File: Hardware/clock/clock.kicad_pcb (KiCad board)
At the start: 2 copper layers, 127.5 x 48 mm, 19 parts, among them J1 Barrel_Jack_Switch, U1 WEMOS_C3_mini, U2 MAX7221xNG, U3 SBC18-11EGWA, U4 LM2596S-5, U5 SBC18-11EGWA, U6 SBC18-11EGWA, U7 SBC18-11EGWA

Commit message: Refactor code structure for improved readability and maintainability
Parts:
- added C10: 100nF, SparkFun-Capacitor:C_0805_2012Metric, B.Cu at (85.8, 122.1)
- added C11: 100nF, SparkFun-Capacitor:C_0805_2012Metric, B.Cu at (164.4, 138.2)
- added C12: 100nF, SparkFun-Capacitor:C_0805_2012Metric, B.Cu at (125.6, 125.6)
- added C6: 100nF, SparkFun-Capacitor:C_0805_2012Metric, B.Cu at (99.5, 110.2)
- added C7: 22uF, Capacitor_SMD:C_0805_2012Metric_Pad1.18x1.45mm_HandSolder, B.Cu at (168.0, 130.8)
- added C8: 100nF, SparkFun-Capacitor:C_0805_2012Metric, B.Cu at (169.0, 128.2)
- added C9: 220uF, Capacitor_THT:C_Radial_D6.3mm_H5.0mm_P2.50mm, B.Cu at (87.1, 126.7)
- added J2: Conn_02x03_Top_Bottom, Connector_IDC:IDC-Header_2x03_P2.54mm_Horizontal, B.Cu at (157.3, 141.3)
- added Q1: BC817, Package_TO_SOT_SMD:SOT-23, B.Cu at (163.4, 130.6)
- added Q2: BC817, Package_TO_SOT_SMD:SOT-23, B.Cu at (154.6, 130.6)
- added R2: 10kΩ, PCM_JLCPCB:R_0805, B.Cu at (158.8, 129.4)
- added R3: 10kΩ, PCM_JLCPCB:R_0805, B.Cu at (158.9, 131.8)
- added R4: 10kΩ, PCM_JLCPCB:R_0805, B.Cu at (164.3, 135.4)
- added REF**: MountingHole_2.2mm_M2_Pad_Via, MountingHole:MountingHole_2.2mm_M2_Pad_Via, F.Cu at (171.2, 144.0)
- added REF**: MountingHole_2.2mm_M2_Pad_Via, MountingHole:MountingHole_2.2mm_M2_Pad_Via, F.Cu at (45.1, 95.7)
- added REF**: MountingHole_2.2mm_M2_Pad_Via, MountingHole:MountingHole_2.2mm_M2_Pad_Via, F.Cu at (171.3, 95.9)
- added REF**: MountingHole_2.2mm_M2_Pad_Via, MountingHole:MountingHole_2.2mm_M2_Pad_Via, F.Cu at (45.5, 143.7)
- added SW1: PTH_RA_h7.5mm, SparkFun-Switch:Push_PTH_RA_8-020_h7.5mm, B.Cu at (171.4, 136.9)
- added U8: LM2596S-5, Package_TO_SOT_SMD:TO-263-5_TabPin3, B.Cu at (52.8, 121.8)
- C1: value 680uF -> 10uF; footprint Capacitor_THT:C_Radial_D8.0mm_H11.5mm_P3.50mm -> Capacitor_SMD:CP_Elec_4x5.4
- C2: value 220uF -> 100nF; footprint Capacitor_THT:C_Radial_D6.3mm_H5.0mm_P2.50mm -> SparkFun-Capacitor:C_0805_2012Metric
- C3: value 104 -> 680uF; footprint Capacitor_THT:C_Disc_D3.0mm_W1.6mm_P2.50mm -> Capacitor_THT:C_Radial_D6.3mm_H7.0mm_P2.50mm
- C4: value 1uF -> 100nF; footprint Capacitor_THT:C_Radial_D4.0mm_H5.0mm_P1.50mm -> SparkFun-Capacitor:C_0805_2012Metric
- C5: value 104 -> 22uF; footprint Capacitor_THT:C_Disc_D3.0mm_W1.6mm_P2.50mm -> SparkFun-Fuse:1206
- D1: value M7 -> Red; footprint PCM_JLCPCB:D_SMA -> LED_THT:LED_D3.0mm; moved to F.Cu
- D2: value SS24 -> Red; footprint PCM_JLCPCB:D_SMA -> LED_THT:LED_D3.0mm; moved to F.Cu
- D3: value Red -> SS34; footprint SparkFun-LED:LED_0603_1608Metric_Red -> Diode_SMD:D_SMA; moved to B.Cu
- D4: value Red -> SS24; footprint SparkFun-LED:LED_0603_1608Metric_Red -> PCM_JLCPCB:D_SMA; moved to B.Cu
- R1: value 10k -> 10kΩ; footprint Resistor_THT:R_Axial_DIN0204_L3.6mm_D1.6mm_P5.08mm_Horizontal -> PCM_JLCPCB:R_0805
- U1: value WEMOS_C3_mini -> SBC18-11EGWA; footprint RF_Module:WEMOS_C3_mini -> Display_7Segment:SBC18-11SURKCGKWA; moved to F.Cu
- U2: value MAX7221xNG -> SBC18-11EGWA; footprint Package_DIP:DIP-24_W7.62mm -> Display_7Segment:SBC18-11SURKCGKWA; moved to F.Cu
- U4: value LM2596S-5 -> ESP32-WROOM-32; footprint Package_TO_SOT_SMD:TO-263-5_TabPin3 -> RF_Module:ESP32-WROOM-32
- U6: value SBC18-11EGWA -> MAX7221xNG; footprint Display_7Segment:SBC18-11SURKCGKWA -> Package_DIP:DIP-24_W7.62mm; moved to B.Cu
- U7: value SBC18-11EGWA -> AMS1117-3.3; footprint Display_7Segment:SBC18-11SURKCGKWA -> Package_TO_SOT_SMD:SOT-223-3_TabPin2; moved to B.Cu
- moved J1 149.2 mm to (58.6, 109.2), turned to 90 degrees
- moved C1 118.7 mm to (85.5, 116.8), turned to 180 degrees
- moved U7 109.9 mm to (89.1, 109.3), turned to 180 degrees
- moved L1 103.5 mm to (75.4, 124.2), turned to -90 degrees
- moved D1 99.7 mm to (106.1, 107.7)
- moved D3 87.9 mm to (62.5, 111.3)
- moved D4 84.6 mm to (65.8, 123.6), turned to -90 degrees
- moved U2 82.8 mm to (75.4, 139.5)
- moved D2 82.0 mm to (106.1, 127.2), turned to 0 degrees
- moved C2 76.6 mm to (91.4, 115.5)
- moved C5 66.3 mm to (96.3, 110.2)
- moved U1 58.2 mm to (45.9, 139.5), turned to 90 degrees
- moved U6 56.6 mm to (113.8, 115.0), turned to -90 degrees
- moved C3 50.2 mm to (68.6, 113.3)
- moved C4 47.6 mm to (65.4, 117.4), turned to 90 degrees
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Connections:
- C1 pad 1: /pwr_in -> +5V
- C3 pad 1: +5V -> /pwr_in
- C4 pad 1: +5V -> /pwr_in
- C5 pad 1: +5V -> 3.3V
- D1 pad 1: /pwr_in -> GND
- D1 pad 2: Net-(D1-Pad2) -> /Sec
- D2 pad 1: Net-(U4-OUT) -> GND
- D2 pad 2: GND -> /Sec
- D3 pad 1: GND -> /pwr_in
- D3 pad 2: /Sec -> Net-(D3-A)
- D4 pad 1: GND -> Net-(U8-OUT)
- D4 pad 2: /Sec -> GND
- J1 pad 1: Net-(D1-Pad2) -> Net-(D3-A)
- L1 pad 1: Net-(U4-OUT) -> Net-(U8-OUT)
- R1 pad 1: +5V -> Net-(U6-ISET)
- R1 pad 2: Net-(U2-ISET) -> +5V
- U1 pad 1: unconnected-(U1-EN-Pad1) -> /DIG_0
- U1 pad 10: GND -> /G
- U1 pad 2: /Sec -> /E
- U1 pad 3: unconnected-(U1-D2-Pad3) -> /D
- U1 pad 4: unconnected-(U1-D1-Pad4) -> /C
- U1 pad 6: unconnected-(U1-D4-Pad6) -> /B
- U1 pad 7: unconnected-(U1-D5-Pad7) -> /A
- U1 pad 9: +5V -> /F
- U2 pad 1: unconnected-(U2-DIN-Pad1) -> /DIG_1
- U2 pad 10: unconnected-(U2-DIG_5-Pad10) -> /G
- U2 pad 2: /DIG_0 -> /E
- U2 pad 3: unconnected-(U2-DIG_4-Pad3) -> /D
- U2 pad 4: GND -> /C
- U2 pad 6: /DIG_2 -> /B
- U2 pad 7: /DIG_3 -> /A
- U2 pad 9: GND -> /F
- U3 pad 1: /DIG_0 -> /DIG_2
- U4 pad 1: /pwr_in -> GND
- U4 pad 2: Net-(U4-OUT) -> 3.3V
- U4 pad 3: GND -> /EN
- U4 pad 4: +5V -> unconnected-(U4-SENSOR_VP-Pad4)
- U4 pad 5: GND -> unconnected-(U4-SENSOR_VN-Pad5)
- U5 pad 1: /DIG_1 -> /DIG_3
- U6 pad 1: /DIG_2 -> /MOSI
- U6 pad 10: /G -> unconnected-(U6-DIG_5-Pad10)
- U6 pad 2: /E -> /DIG_0
- U6 pad 3: /D -> unconnected-(U6-DIG_4-Pad3)
- U6 pad 4: /C -> GND
- U6 pad 6: /B -> /DIG_2
- U6 pad 7: /A -> /DIG_3
- U6 pad 9: /F -> GND
- U7 pad 1: /DIG_3 -> GND
- U7 pad 2: /E -> 3.3V
- U7 pad 3: /D -> +5V
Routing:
- net 3.3V: track 0.00 -> 107.1 mm
- net GND: track 11.1 -> 76.0 mm, vias 5 -> 15
- net /MOSI: track 0.00 -> 63.6 mm
- net /Sec: track 86.5 -> 27.1 mm, vias 0 -> 1
- net /DIG_1: track 13.8 -> 65.3 mm, vias 0 -> 1
- net /RXD0: track 0.00 -> 40.1 mm, vias 0 -> 1
- net /B: track 127.5 -> 164.6 mm
- net /TXD0: track 0.00 -> 34.9 mm, vias 0 -> 1
- net /CLK: track 0.00 -> 34.9 mm, vias 0 -> 2
- net /EN: track 0.00 -> 30.2 mm, vias 0 -> 2
- net /IO0: track 0.00 -> 30.0 mm
- net +5V: track 123.2 -> 150.6 mm
- net /E: track 128.3 -> 154.4 mm, vias 2 -> 3
- net /DIG_3: track 59.2 -> 33.3 mm, vias 1 -> 0
- net /CS: track 0.00 -> 23.4 mm
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- removed copper zone on B.Cu, net /pwr_in
- removed copper zone on B.Cu, net GND
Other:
- board size 127.5 x 48 mm -> 131.8 x 53.9 mm

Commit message: Refactor code structure for improved readability and maintainability
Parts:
- removed J2: Conn_02x03_Top_Bottom, Connector_IDC:IDC-Header_2x03_P2.54mm_Horizontal
- added J3: Conn_02x03_Odd_Even, Connector_IDC:IDC-Header_2x03_P2.54mm_Horizontal, F.Cu at (162.5, 141.1)
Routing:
- net /pwr_in: track 18.3 -> 0.10 mm
- net /TXD0: track 34.9 -> 43.6 mm
- net 3.3V: track 107.1 -> 99.2 mm
- net GND: track 76.0 -> 82.9 mm
- net /DTR: track 13.5 -> 18.6 mm
- net /RXD0: track 40.1 -> 35.1 mm
- net +5V: track 150.6 -> 146.6 mm
- net Net-(D3-A): track 3.97 -> 0.10 mm
- net /DIG_1: track 65.3 -> 67.0 mm
- net /DIG_2: track 28.1 -> 29.7 mm
- net /CLK: track 34.9 -> 35.9 mm
- net /RTS: track 19.7 -> 18.7 mm

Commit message: Updated README.md
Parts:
- added D5: LED, SparkFun-LED:LED_0603_1608Metric, B.Cu at (148.4, 108.9)
- added J2: Conn_01x05_Pin, Connector_PinHeader_2.54mm:PinHeader_1x05_P2.54mm_Vertical, F.Cu at (136.5, 143.1)
- added J4: Conn_01x02_Pin, Connector_PinHeader_2.00mm:PinHeader_1x02_P2.00mm_Vertical, F.Cu at (166.8, 96.8)
- added J5: Conn_01x06_Pin, Connector_PinSocket_2.54mm:PinSocket_1x06_P2.54mm_Vertical, F.Cu at (148.8, 80.6)
- added R5: 1.5k, SparkFun-Resistor:R_0603_1608Metric, B.Cu at (148.5, 112.7)
- added R6: 4.7k, SparkFun-Resistor:R_0603_1608Metric, F.Cu at (167.3, 100.5)
- added R7: 4.7k, SparkFun-Resistor:R_0603_1608Metric, F.Cu at (164.4, 100.6)
- J3: footprint Connector_IDC:IDC-Header_2x03_P2.54mm_Horizontal -> Connector_PinHeader_2.54mm:PinHeader_1x06_P2.54mm_Vertical
- moved J3 3.34 mm to (164.4, 143.8)
- moved J1 1.62 mm to (56.9, 109.2)
- moved D3 1.27 mm to (61.2, 111.3)
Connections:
- U4 pad 13: unconnected-(U4-IO14-Pad13) -> /14
- U4 pad 14: unconnected-(U4-IO12-Pad14) -> /12
- U4 pad 16: unconnected-(U4-IO13-Pad16) -> /13
- U4 pad 23: unconnected-(U4-IO15-Pad23) -> /15
- U4 pad 24: unconnected-(U4-IO2-Pad24) -> /2
- U4 pad 27: unconnected-(U4-IO16-Pad27) -> /16
- U4 pad 33: unconnected-(U4-IO21-Pad33) -> /SDA
- U4 pad 36: unconnected-(U4-IO22-Pad36) -> /SCL
- U4 pad 6: unconnected-(U4-IO34-Pad6) -> /ADC_3
- U4 pad 7: unconnected-(U4-IO35-Pad7) -> /ADC_4
- U4 pad 8: unconnected-(U4-IO32-Pad8) -> /ADC_1
- U4 pad 9: unconnected-(U4-IO33-Pad9) -> /ADC_2
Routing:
- net /ADC_1: track 0.00 -> 37.6 mm, vias 0 -> 2
- net /ADC_3: track 0.00 -> 34.9 mm, vias 0 -> 2
- net /ADC_2: track 0.00 -> 33.4 mm, vias 0 -> 2
- net /ADC_4: track 0.00 -> 31.2 mm, vias 0 -> 2
- net 3.3V: track 99.2 -> 130.2 mm, vias 0 -> 1
- net /SDA: track 0.00 -> 17.2 mm, vias 0 -> 3
- net /SCL: track 0.00 -> 13.8 mm, vias 0 -> 1
- net GND: track 82.9 -> 70.7 mm, vias 15 -> 17
- net /2: track 0.00 -> 10.8 mm, vias 0 -> 2
- net /RXD0: track 35.1 -> 45.4 mm
- net +5V: track 146.6 -> 154.1 mm
- net /TXD0: track 43.6 -> 48.5 mm
- net Net-(D5-A): track 0.00 -> 2.39 mm
- net /DTR: track 18.6 -> 20.7 mm, vias 1 -> 2
- net /MOSI: track 63.6 -> 64.9 mm
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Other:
- board text added: "5V"
- board text added: "AN_1"
- board text added: "AN_2"
- board text added: "AN_3"
- board text added: "AN_4"
- board text added: "DTR"
- board text added: "GND"
- board text added: "RST"
- board text added: "RX"
- board text added: "TX"

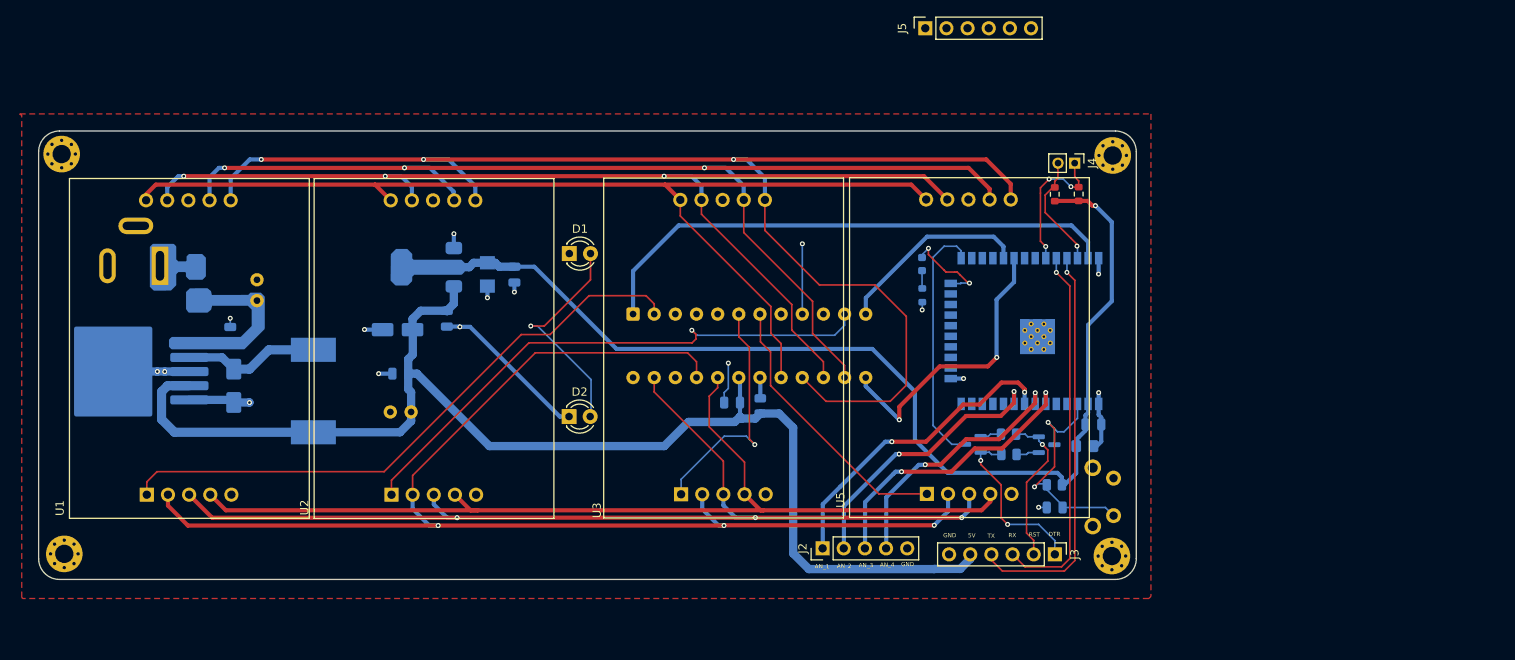
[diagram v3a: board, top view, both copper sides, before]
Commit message: Add initial PCB lock file and component list for clock project
- Created a lock file for the PCB design with hostname and username.
- Added a comprehensive CSV file listing components for the clock project, including values, footprints, and datasheets for each component.
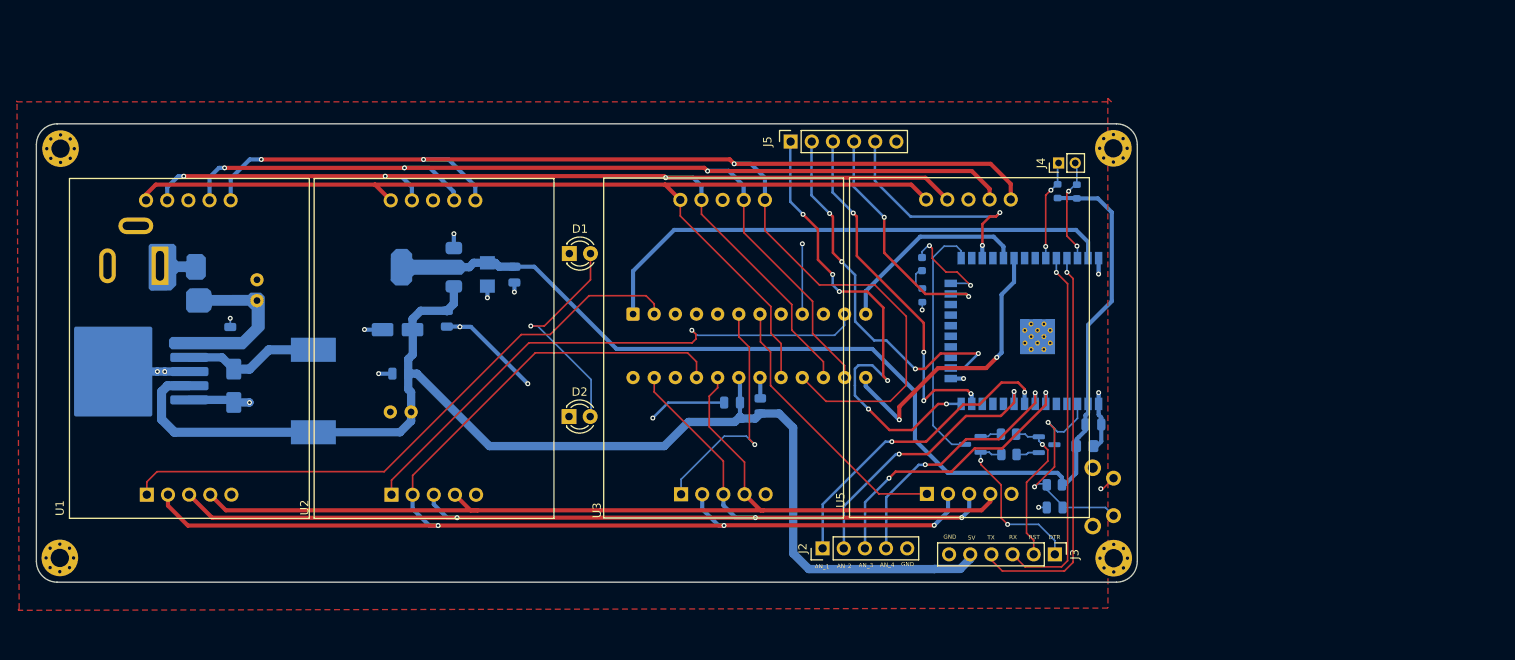
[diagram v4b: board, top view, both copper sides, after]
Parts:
- R6, R7: moved to B.Cu
- moved J5 21.1 mm to (132.7, 94.2)
- moved R7 2.67 mm to (167.0, 100.2)
- moved R6 2.55 mm to (164.7, 100.2)
- moved J4 1.93 mm to (164.8, 96.8), turned to 90 degrees
- moved REF** 0.86 mm to (171.4, 95.0)
- moved REF** 0.72 mm to (44.9, 144.2)
- moved REF** 0.67 mm to (45.0, 95.1)
- moved REF** 0.34 mm to (171.5, 144.3)
- turned D5 to 90 degrees
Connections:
- D5 pad 1: /2 -> Net-(D5-K)
- D5 pad 2: Net-(D5-A) -> /2
- J5 pad 1: unconnected-(J5-Pin_1-Pad1) -> /12
- J5 pad 2: unconnected-(J5-Pin_2-Pad2) -> /13
- J5 pad 3: unconnected-(J5-Pin_3-Pad3) -> /14
- J5 pad 4: unconnected-(J5-Pin_4-Pad4) -> /15
- J5 pad 5: unconnected-(J5-Pin_5-Pad5) -> /16
- J5 pad 6: unconnected-(J5-Pin_6-Pad6) -> GND
- R5 pad 1: Net-(D5-A) -> Net-(D5-K)
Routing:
- net /12: track 0.00 -> 59.4 mm, vias 0 -> 6
- net /13: track 0.00 -> 45.7 mm, vias 0 -> 4
- net /14: track 0.00 -> 43.3 mm, vias 0 -> 4
- net /15: track 0.00 -> 29.5 mm, vias 0 -> 2
- net /16: track 0.00 -> 28.5 mm, vias 0 -> 2
- net /SDA: track 17.2 -> 12.1 mm, vias 3 -> 2
- net Net-(D5-K): track 0.00 -> 3.37 mm
- net Net-(D5-A): track 2.39 -> 0.00 mm
- net /2: track 10.8 -> 12.0 mm
- net /SCL: track 13.8 -> 12.9 mm, vias 1 -> 2
- net /A: track 141.1 -> 140.6 mm
- net 3.3V: track 130.2 -> 130.6 mm, vias 1 -> 0
- net GND: track 70.7 -> 70.5 mm, vias 17 -> 19
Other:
- board size 131.8 x 53.9 mm -> 132.2 x 55 mm
